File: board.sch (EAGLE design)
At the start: 1 part

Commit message: Add files via upload
Started creating the board
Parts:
- added C1: 100uF, steves:CPOLTANT02
- added CON1: Power, steves:CON-1X2WEID-PCB
- added R1, R2, R3, R4, R5: 10k, resistor:R-US_R0805
- added R6: 470, resistor:R-US_R0805
- added SW1: PROG, steves:SWITCH-PUSHBUTTONSMD
- added SW2: RESET, steves:SWITCH-PUSHBUTTONSMD
- MDL1: value (none) -> ESP8266
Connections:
- new net GND: C1.NEGATIVE, CON1.2, MDL1.GND, R1.2, R6.1, SW2.P$3, SW2.P$4
- new net N$1: MDL1.GPIO15, R1.1
- new net N$2: MDL1.GPIO2, R4.1
- new net N$3: MDL1.CH_PD, R3.2
- new net N$5: MDL1.GPIO16, MDL1.REST, R5.2, SW2.P$1, SW2.P$2
- new net N$6: MDL1.GPIO0, R2.1, SW1.P$3, SW1.P$4
- new net N$7: R6.2, SW1.P$1, SW1.P$2
- new net VCC: C1.POSITIVE, CON1.1, MDL1.VCC, R2.2, R3.1, R4.2, R5.1
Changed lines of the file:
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@@
 <layer number="97" name="Info" color="7" fill="1" visible="yes" active="yes"/>
 <layer number="98" name="Guide" color="6" fill="1" visible="yes" active="yes"/>
+<layer number="99" name="SpiceOrder" color="5" fill="1" visible="yes" active="yes"/>
+<layer number="101" name="Hidden" color="15" fill="1" visible="yes" active="yes"/>
+<layer number="102" name="Changes" color="12" fill="1" visible="yes" active="yes"/>
+<layer number="250" name="Descript" color="3" fill="1" visible="no" active="no"/>
+<layer number="251" name="SMDround" color="4" fill="9" visible="no" active="yes"/>
 </layers>
 <schematic xreflabel="%F%N/%S.%C%R" xrefpart="/%S.%C%R">
@@
 </classes>
 <parts>
-<part name="MDL1" library="ESP12E" deviceset="ESP8266-12E" device="ESP8266-ESP12E"/>
+<part name="MDL1" library="ESP12E" deviceset="ESP8266-12E" device="ESP8266-ESP12E" value="ESP8266"/>
+<part name="R1" library="resistor" deviceset="R-US_" device="R0805" value="10k"/>
+<part name="R2" library="resistor" deviceset="R-US_" device="R0805" value="10k"/>
+<part name="R3" library="resistor" deviceset="R-US_" device="R0805" value="10k"/>
+<part name="GND1" library="supply1" deviceset="GND" device=""/>
+<part name="P+1" library="supply1" deviceset="VCC" device=""/>
+<part name="P+2" library="supply1" deviceset="VCC" device=""/>
+<part name="R4" library="resistor" deviceset="R-US_" device="R0805" value="10k"/>
+<part name="R5" library="resistor" deviceset="R-US_" device="R0805" value="10k"/>
+<part name="R6" library="resistor" deviceset="R-US_" device="R0805" value="470"/>
+<part name="SW1" library="steves" deviceset="SWITCH-PUSHBUTTON" device="SMD" value="PROG"/>
+<part name="FRAME1" library="frames" deviceset="DINA4_L" device="" value="Test project"/>
+<part name="CON1" library="steves" deviceset="CON-1X2" device="WEID-PCB" value="Power"/>
+<part name="C1" library="steves" deviceset="CPOL" device="TANT02" value="100uF"/>
+<part name="P+3" library="supply1" deviceset="VCC" device=""/>
+<part name="GND2" library="supply1" deviceset="GND" device=""/>
+<part name="SW2" library="steves" deviceset="SWITCH-PUSHBUTTON" device="SMD" value="RESET"/>
 </parts>
 <sheets>
@@
 <instances>
 <instance part="MDL1" gate="G$1" x="50.8" y="91.44"/>
+<instance part="R1" gate="G$1" x="71.12" y="81.28"/>
+<instance part="R2" gate="G$1" x="91.44" y="93.98"/>
+<instance part="R3" gate="G$1" x="17.78" y="93.98"/>
+<instance part="GND1" gate="1" x="76.2" y="68.58"/>
+<instance part="P+1" gate="VCC" x="96.52" y="101.6"/>
+<instance part="P+2" gate="VCC" x="10.16" y="106.68"/>
+<instance part="R4" gate="G$1" x="91.44" y="86.36"/>
+<instance part="R5" gate="G$1" x="20.32" y="101.6"/>
+<instance part="R6" gate="G$1" x="83.82" y="71.12"/>
+<instance part="SW1" gate="G$1" x="99.06" y="71.12"/>
+<instance part="FRAME1" gate="G$1" x="-38.1" y="-5.08"/>
+<instance part="FRAME1" gate="G$2" x="124.46" y="-5.08"/>
+<instance part="CON1" gate="G$1" x="101.6" y="96.52"/>
+<instance part="C1" gate="G$1" x="121.92" y="96.52"/>
+<instance part="P+3" gate="VCC" x="111.76" y="106.68"/>
+<instance part="GND2" gate="1" x="111.76" y="83.82"/>
+<instance part="SW2" gate="G$1" x="33.02" y="55.88"/>
 </instances>
 <busses>
 </busses>
 <nets>
+<net name="N$3" class="0">
+<segment>
+<pinref part="MDL1" gate="G$1" pin="CH_PD"/>
+<pinref part="R3" gate="G$1" pin="2"/>
+<wire x1="22.86" y1="93.98" x2="27.94" y2="93.98" width="0.1524" layer="91"/>
+</segment>
+</net>
+<net name="VCC" class="0">
+<segment>
+<pinref part="P+1" gate="VCC" pin="VCC"/>
+<wire x1="96.52" y1="99.06" x2="96.52" y2="93.98" width="0.1524" layer="91"/>
+<pinref part="R2" gate="G$1" pin="2"/>
+<pinref part="R4" gate="G$1" pin="2"/>
+<wire x1="96.52" y1="86.36" x2="96.52" y2="93.98" width="0.1524" layer="91"/>
+<junction x="96.52" y="86.36"/>
+<junction x="96.52" y="93.98"/>
+</segment>
+<segment>
+<pinref part="R3" gate="G$1" pin="1"/>
+<pinref part="P+2" gate="VCC" pin="VCC"/>
+<wire x1="12.7" y1="93.98" x2="10.16" y2="93.98" width="0.1524" layer="91"/>
+<wire x1="10.16" y1="93.98" x2="10.16" y2="101.6" width="0.1524" layer="91"/>
+<junction x="10.16" y="93.98"/>
+<pinref part="MDL1" gate="G$1" pin="VCC"/>
+<wire x1="10.16" y1="101.6" x2="10.16" y2="104.14" width="0.1524" layer="91"/>
+<wire x1="27.94" y1="81.28" x2="10.16" y2="81.28" width="0.1524" layer="91"/>
+<wire x1="10.16" y1="81.28" x2="10.16" y2="93.98" width="0.1524" layer="91"/>
+<pinref part="R5" gate="G$1" pin="1"/>
+<wire x1="15.24" y1="101.6" x2="10.16" y2="101.6" width="0.1524" layer="91"/>
+<junction x="10.16" y="101.6"/>
+</segment>
+<segment>
+<pinref part="P+3" gate="VCC" pin="VCC"/>
+<wire x1="111.76" y1="104.14" x2="111.76" y2="101.6" width="0.1524" layer="91"/>
+<pinref part="CON1" gate="G$1" pin="1"/>
+<wire x1="111.76" y1="101.6" x2="111.76" y2="96.52" width="0.1524" layer="91"/>
+<wire x1="111.76" y1="96.52" x2="104.14" y2="96.52" width="0.1524" layer="91"/>
+<pinref part="C1" gate="G$1" pin="POSITIVE"/>
+<wire x1="121.92" y1="99.06" x2="121.92" y2="101.6" width="0.1524" layer="91"/>
+<wire x1="121.92" y1="101.6" x2="111.76" y2="101.6" width="0.1524" layer="91"/>
+<junction x="111.76" y="101.6"/>
+</segment>
+</net>
+<net name="GND" class="0">
+<segment>
+<pinref part="R1" gate="G$1" pin="2"/>
+<pinref part="GND1" gate="1" pin="GND"/>
+<wire x1="76.2" y1="81.28" x2="76.2" y2="76.2" width="0.1524" layer="91"/>
+<pinref part="MDL1" gate="G$1" pin="GND"/>
+<wire x1="76.2" y1="76.2" x2="76.2" y2="71.12" width="0.1524" layer="91"/>
+<wire x1="60.96" y1="81.28" x2="63.5" y2="81.28" width="0.1524" layer="91"/>
+<wire x1="63.5" y1="81.28" x2="63.5" y2="76.2" width="0.1524" layer="91"/>
+<wire x1="63.5" y1="76.2" x2="76.2" y2="76.2" width="0.1524" layer="91"/>
+<junction x="76.2" y="76.2"/>
+<pinref part="R6" gate="G$1" pin="1"/>
+<wire x1="78.74" y1="71.12" x2="76.2" y2="71.12" width="0.1524" layer="91"/>
+<junction x="76.2" y="71.12"/>
+<pinref part="SW2" gate="G$1" pin="P$3"/>
+<pinref part="SW2" gate="G$1" pin="P$4"/>
+<wire x1="38.1" y1="58.42" x2="38.1" y2="55.88" width="0.1524" layer="91"/>
+<wire x1="38.1" y1="58.42" x2="63.5" y2="58.42" width="0.1524" layer="91"/>
+<junction x="38.1" y="58.42"/>
+<wire x1="63.5" y1="58.42" x2="63.5" y2="76.2" width="0.1524" layer="91"/>
+<junction x="63.5" y="76.2"/>
+</segment>
+<segment>
+<pinref part="CON1" gate="G$1" pin="2"/>
+<wire x1="104.14" y1="93.98" x2="111.76" y2="93.98" width="0.1524" layer="91"/>
+<pinref part="GND2" gate="1" pin="GND"/>
+<wire x1="111.76" y1="93.98" x2="111.76" y2="88.9" width="0.1524" layer="91"/>
+<pinref part="C1" gate="G$1" pin="NEGATIVE"/>
+<wire x1="111.76" y1="88.9" x2="111.76" y2="86.36" width="0.1524" layer="91"/>
+<wire x1="121.92" y1="91.44" x2="121.92" y2="88.9" width="0.1524" layer="91"/>
+<wire x1="121.92" y1="88.9" x2="111.76" y2="88.9" width="0.1524" layer="91"/>
+<junction x="111.76" y="88.9"/>
+</segment>
+</net>
+<net name="N$1" class="0">
+<segment>
+<pinref part="MDL1" gate="G$1" pin="GPIO15"/>
+<wire x1="60.96" y1="83.82" x2="66.04" y2="83.82" width="0.1524" layer="91"/>
+<pinref part="R1" gate="G$1" pin="1"/>
+<wire x1="66.04" y1="83.82" x2="66.04" y2="81.28" width="0.1524" layer="91"/>
+</segment>
+</net>
+<net name="N$7" class="0">
+<segment>
+<pinref part="R6" gate="G$1" pin="2"/>
+<pinref part="SW1" gate="G$1" pin="P$2"/>
+<wire x1="88.9" y1="71.12" x2="91.44" y2="71.12" width="0.1524" layer="91"/>
+<pinref part="SW1" gate="G$1" pin="P$1"/>
+<wire x1="91.44" y1="71.12" x2="93.98" y2="71.12" width="0.1524" layer="91"/>
+<wire x1="93.98" y1="73.66" x2="91.44" y2="73.66" width="0.1524" layer="91"/>
+<wire x1="91.44" y1="73.66" x2="91.44" y2="71.12" width="0.1524" layer="91"/>
+<junction x="91.44" y="71.12"/>
+</segment>
+</net>
+<net name="N$6" class="0">
+<segment>
+<pinref part="R2" gate="G$1" pin="1"/>
+<wire x1="81.28" y1="88.9" x2="81.28" y2="93.98" width="0.1524" layer="91"/>
+<wire x1="81.28" y1="93.98" x2="86.36" y2="93.98" width="0.1524" layer="91"/>
+<pinref part="MDL1" gate="G$1" pin="GPIO0"/>
+<wire x1="60.96" y1="88.9" x2="81.28" y2="88.9" width="0.1524" layer="91"/>
+<wire x1="81.28" y1="88.9" x2="81.28" y2="81.28" width="0.1524" layer="91"/>
+<junction x="81.28" y="88.9"/>
+<pinref part="SW1" gate="G$1" pin="P$3"/>
+<wire x1="106.68" y1="73.66" x2="104.14" y2="73.66" width="0.1524" layer="91"/>
+<pinref part="SW1" gate="G$1" pin="P$4"/>
+<wire x1="104.14" y1="71.12" x2="106.68" y2="71.12" width="0.1524" layer="91"/>
+<wire x1="106.68" y1="71.12" x2="106.68" y2="73.66" width="0.1524" layer="91"/>
+<wire x1="81.28" y1="81.28" x2="106.68" y2="81.28" width="0.1524" layer="91"/>
+<wire x1="106.68" y1="81.28" x2="106.68" y2="73.66" width="0.1524" layer="91"/>
+<junction x="106.68" y="73.66"/>
+</segment>
+</net>
+<net name="N$2" class="0">
+<segment>
+<pinref part="MDL1" gate="G$1" pin="GPIO2"/>
+<pinref part="R4" gate="G$1" pin="1"/>
+<wire x1="60.96" y1="86.36" x2="86.36" y2="86.36" width="0.1524" layer="91"/>
+</segment>
+</net>
+<net name="N$5" class="0">
+<segment>
+<pinref part="SW2" gate="G$1" pin="P$2"/>
+<pinref part="SW2" gate="G$1" pin="P$1"/>
+<wire x1="27.94" y1="55.88" x2="27.94" y2="58.42" width="0.1524" layer="91"/>
+<pinref part="MDL1" gate="G$1" pin="GPIO16"/>
+<wire x1="27.94" y1="91.44" x2="25.4" y2="91.44" width="0.1524" layer="91"/>
+<wire x1="25.4" y1="91.44" x2="25.4" y2="99.06" width="0.1524" layer="91"/>
+<pinref part="MDL1" gate="G$1" pin="REST"/>
+<wire x1="25.4" y1="99.06" x2="27.94" y2="99.06" width="0.1524" layer="91"/>
+<wire x1="25.4" y1="99.06" x2="25.4" y2="101.6" width="0.1524" layer="91"/>
+<junction x="25.4" y="99.06"/>
+<pinref part="R5" gate="G$1" pin="2"/>
+<junction x="25.4" y="101.6"/>
+<wire x1="27.94" y1="58.42" x2="25.4" y2="58.42" width="0.1524" layer="91"/>
+<wire x1="25.4" y1="58.42" x2="25.4" y2="91.44" width="0.1524" layer="91"/>
+<junction x="27.94" y="58.42"/>
+<junction x="25.4" y="91.44"/>
+</segment>
+</net>
 </nets>
 </sheet>

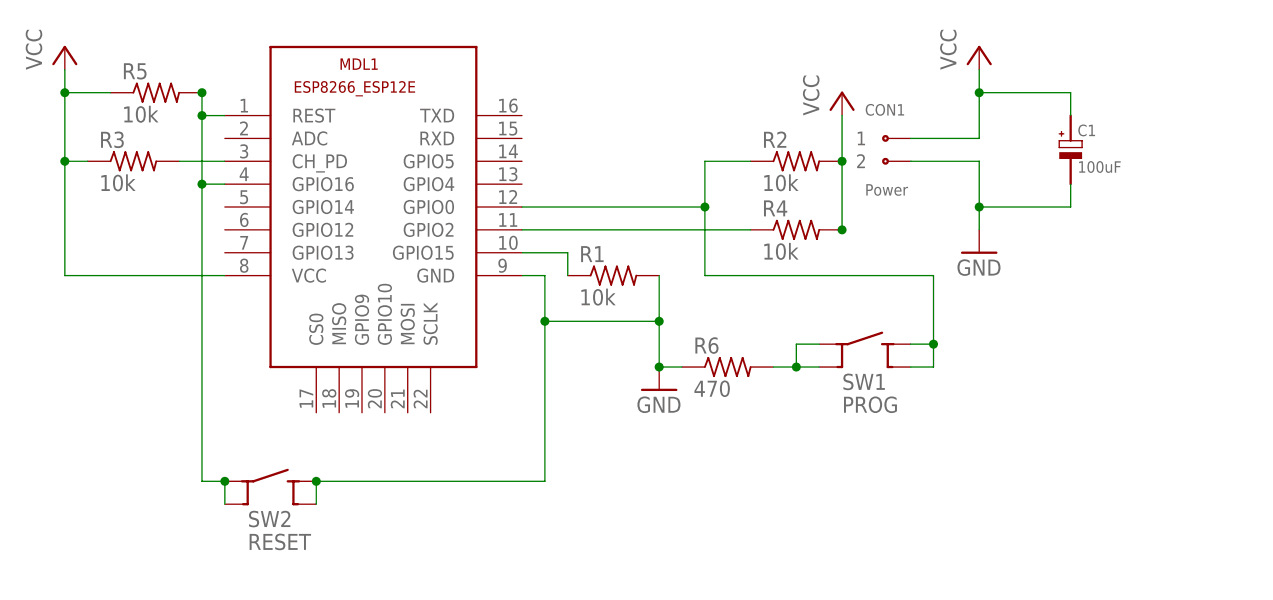
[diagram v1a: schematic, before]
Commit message: Modifications last MHV meeting.
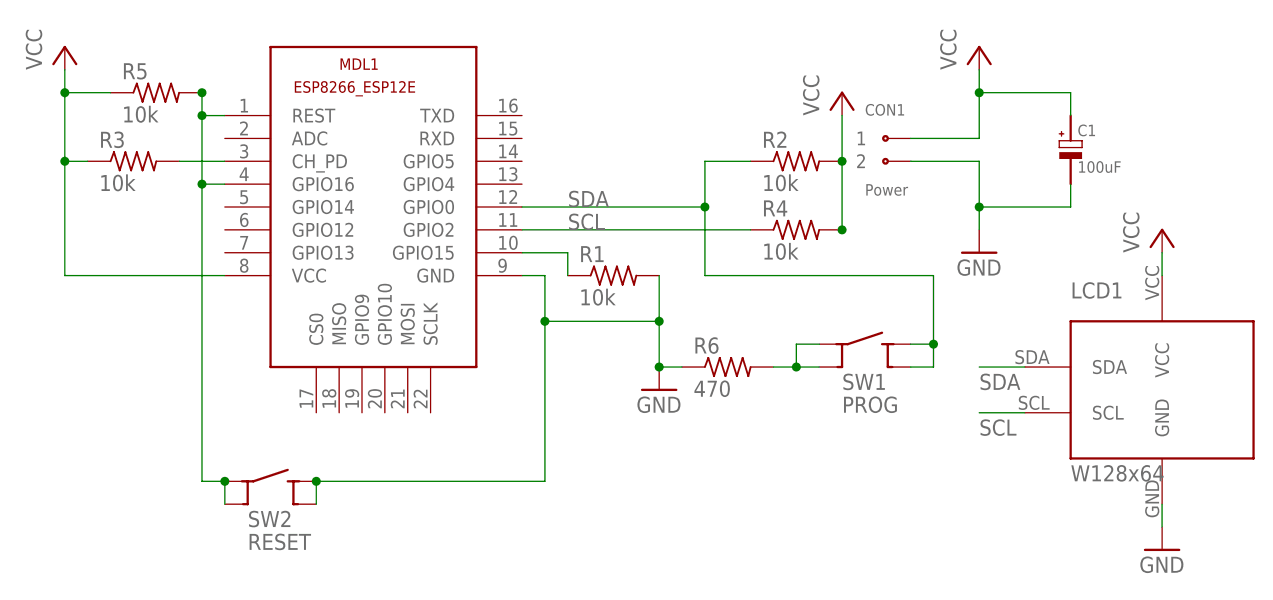
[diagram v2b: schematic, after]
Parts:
- added LCD1: W128x64, my_lib:OLED_64X128
- SW1, SW2: device steves:SWITCH-PUSHBUTTONSMD -> steves:SWITCH-PUSHBUTTONJAYCAR
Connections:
- removed net N$2: MDL1.GPIO2, R4.1
- removed net N$6: MDL1.GPIO0, R2.1, SW1.P$3, SW1.P$4
- new net SCL: LCD1.SCL, MDL1.GPIO2, R4.1
- new net SDA: LCD1.SDA, MDL1.GPIO0, R2.1, SW1.P$3, SW1.P$4
- net GND: now also LCD1.GND
- net VCC: now also LCD1.VCC
